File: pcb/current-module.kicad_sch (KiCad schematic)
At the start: 16 parts, among them J1 Power, J2 QWICC

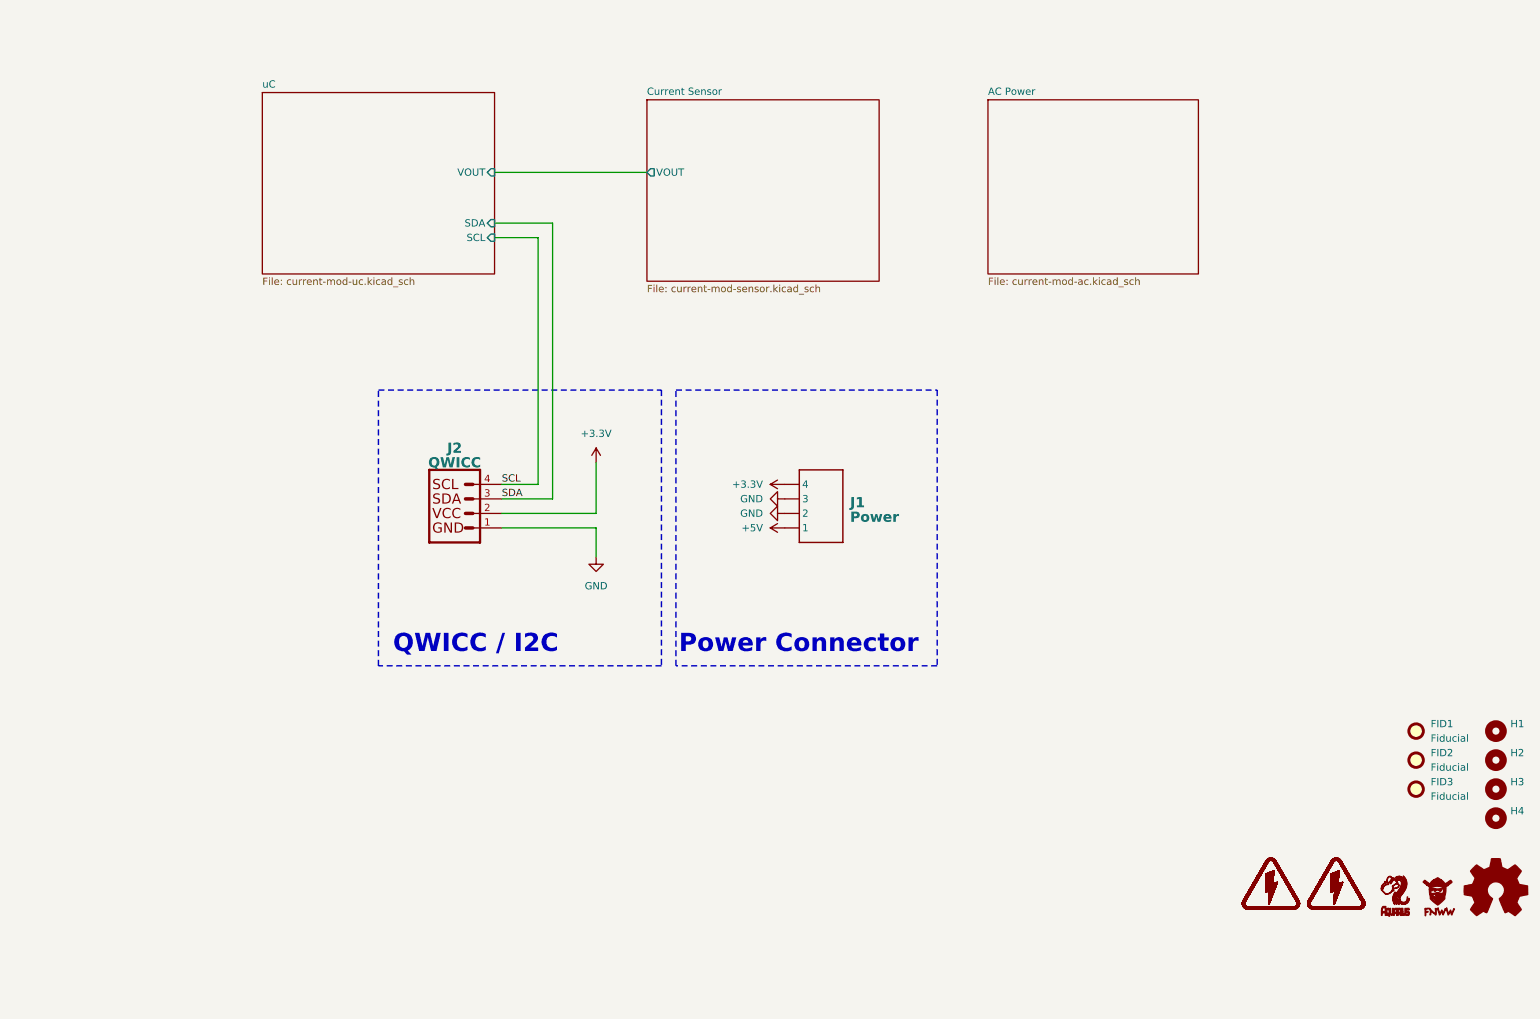
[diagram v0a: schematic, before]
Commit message: Reworked to be headless module
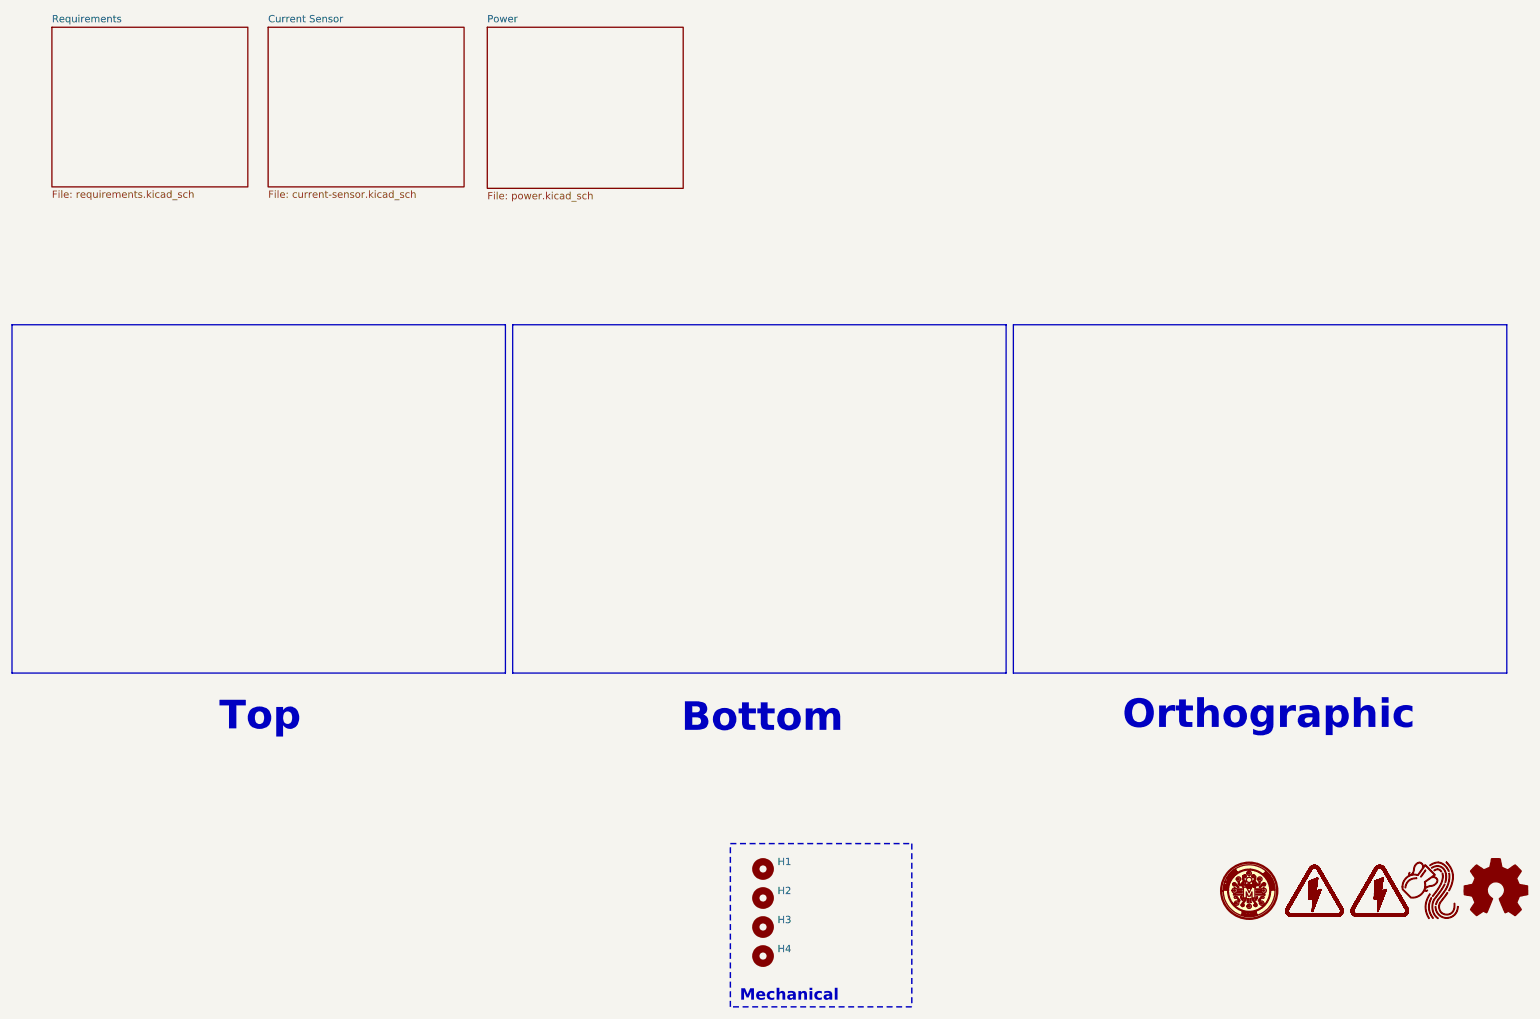
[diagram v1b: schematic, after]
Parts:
- removed FID1, FID2, FID3: Fiducial, Fiducial:Fiducial_0.75mm_Mask1.5mm, symbol Mechanical:Fiducial
- removed J1: Power, Connector_JST:JST_SH_SM04B-SRSS-TB_1x04-1MP_P1.00mm_Horizontal, symbol CRGM Connector:JST-SH-4
- removed J2: QWICC, Connector_JST:JST_SH_SM04B-SRSS-TB_1x04-1MP_P1.00mm_Horizontal, symbol CRGM Connector:QWIIC
- removed LOGO2: ~, CRGM Logos:Aquarius Name 2mmx5mm, symbol CRGM Logos:Aquarius Name
- removed LOGO3: ~, CRGM Logos:FNWW Face 5mm, symbol CRGM Logos:FNWW Face
- removed LOGO4: ~, CRGM Logos:FNWW Name 2mmx5mm, symbol CRGM Logos:FNWW Name
- added LOGO1: ~, CRGM Logos:CRGM Logo 3.5, symbol CRGM Logos:CRGM Logo
- H1, H2, H3, H4: value MountingHole -> ~
- LOGO4: renamed from LOGO5; value Logo_Open_Hardware_Small -> ~; footprint Symbol:OSHW-Symbol_6.7x6mm_SilkScreen -> Symbol:OSHW-Logo_5.7x6mm_SilkScreen
- renumbered LOGO1 to LOGO3, S2 to S1, S1 to S2
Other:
- sheet AC Power renamed Power
- removed sheet uC
- added sheet Requirements (requirements.kicad_sch)
- sheet Current Sensor: file current-mod-sensor.kicad_sch -> current-sensor.kicad_sch
- sheet Current Sensor ports: added none; removed VOUT
- sheet Power: file current-mod-ac.kicad_sch -> power.kicad_sch
- note added: "Bottom"
- note added: "Mechanical"
- note added: "Orthographic"
- note added: "Top"
- note removed: "Power Connector"
- note removed: "QWICC / I2C"
- title: (none) -> Current Detector
